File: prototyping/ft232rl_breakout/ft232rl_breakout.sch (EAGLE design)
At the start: 17 parts, among them J1 USB, U1 FT232RL

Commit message: Performed final auto routing.
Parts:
- removed L1, L2: LED, ft232rl_breakout:LED
- added D1: RED, ft232rl_breakout:LED
- added D2: GREEN, ft232rl_breakout:LED
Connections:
- net N$1 renamed VCC
- net N$16 renamed 3V3
- net VUSB renamed 5V
- net N$2: now also D1.C; no longer L1.C
- net N$3: now also D2.C; no longer L2.C
- net N$4: now also D1.A; no longer L1.A
- net N$5: now also D2.A; no longer L2.A
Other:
- note added: "1"
- note removed: "A"
- moved on the sheet: C1, C2, C3, C4, J1, JP1, JP2, JP3, JP4, JP5, JP6, JP7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

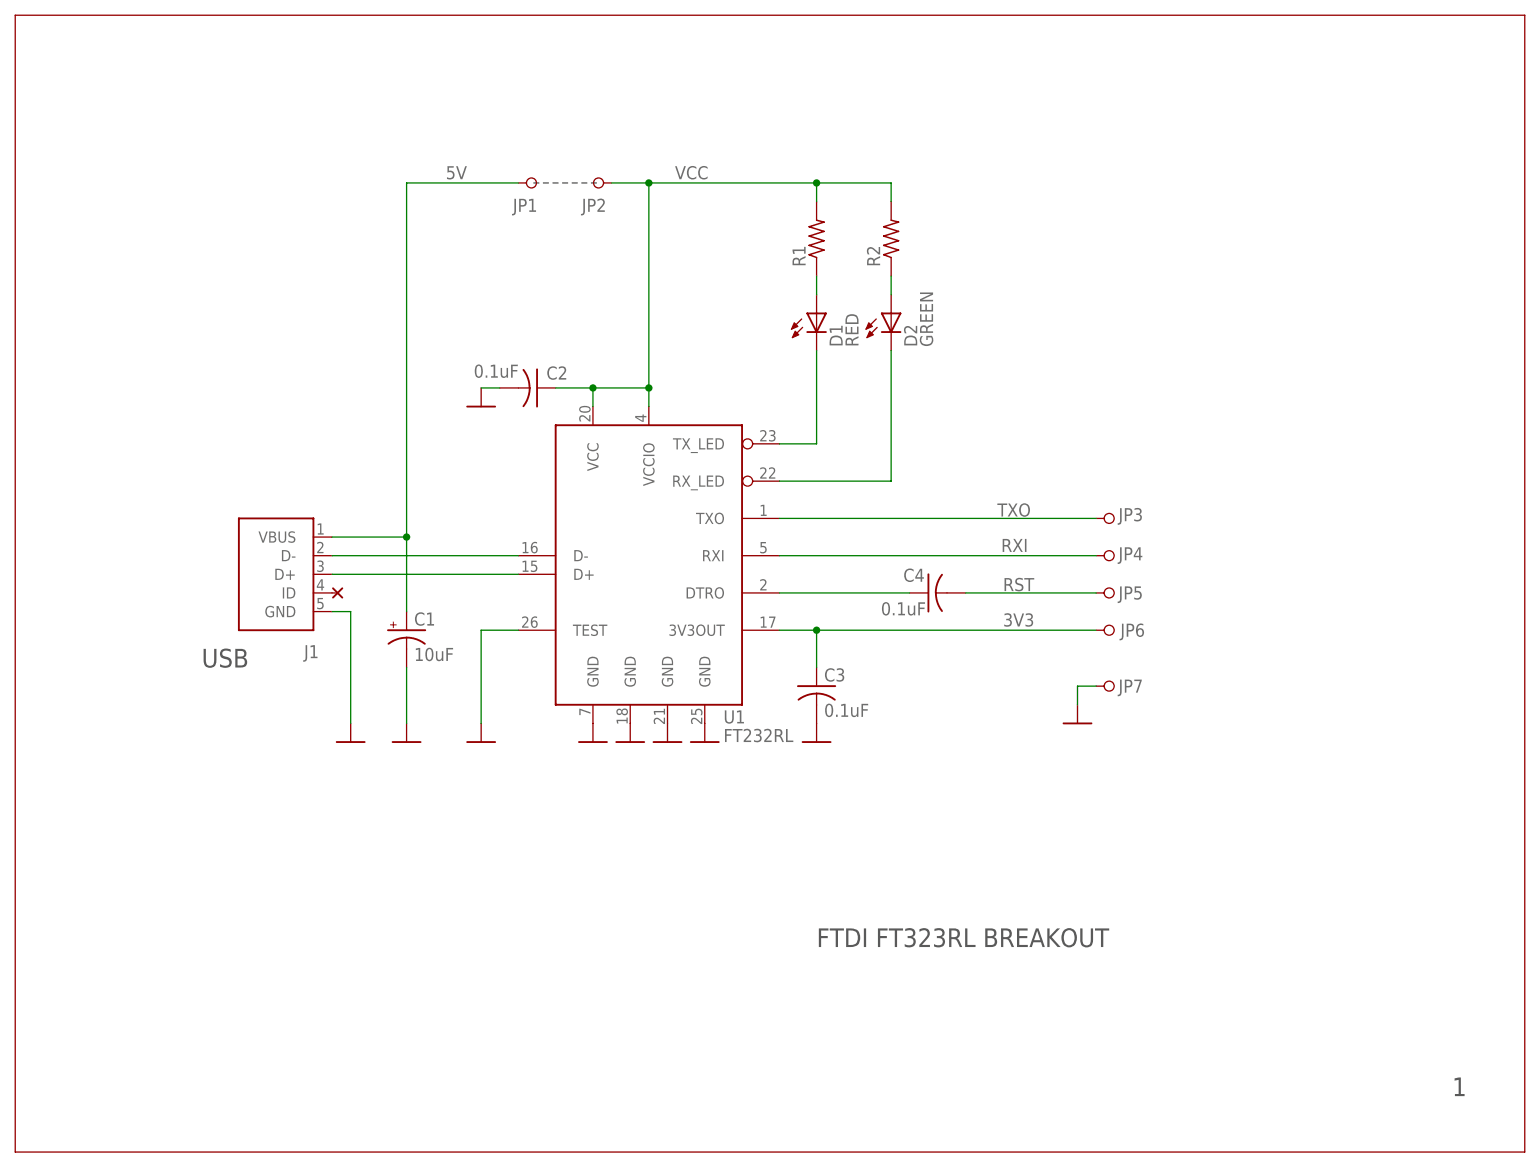
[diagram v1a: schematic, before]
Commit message: Added tcream holes for usb connector tabs. Added bom.
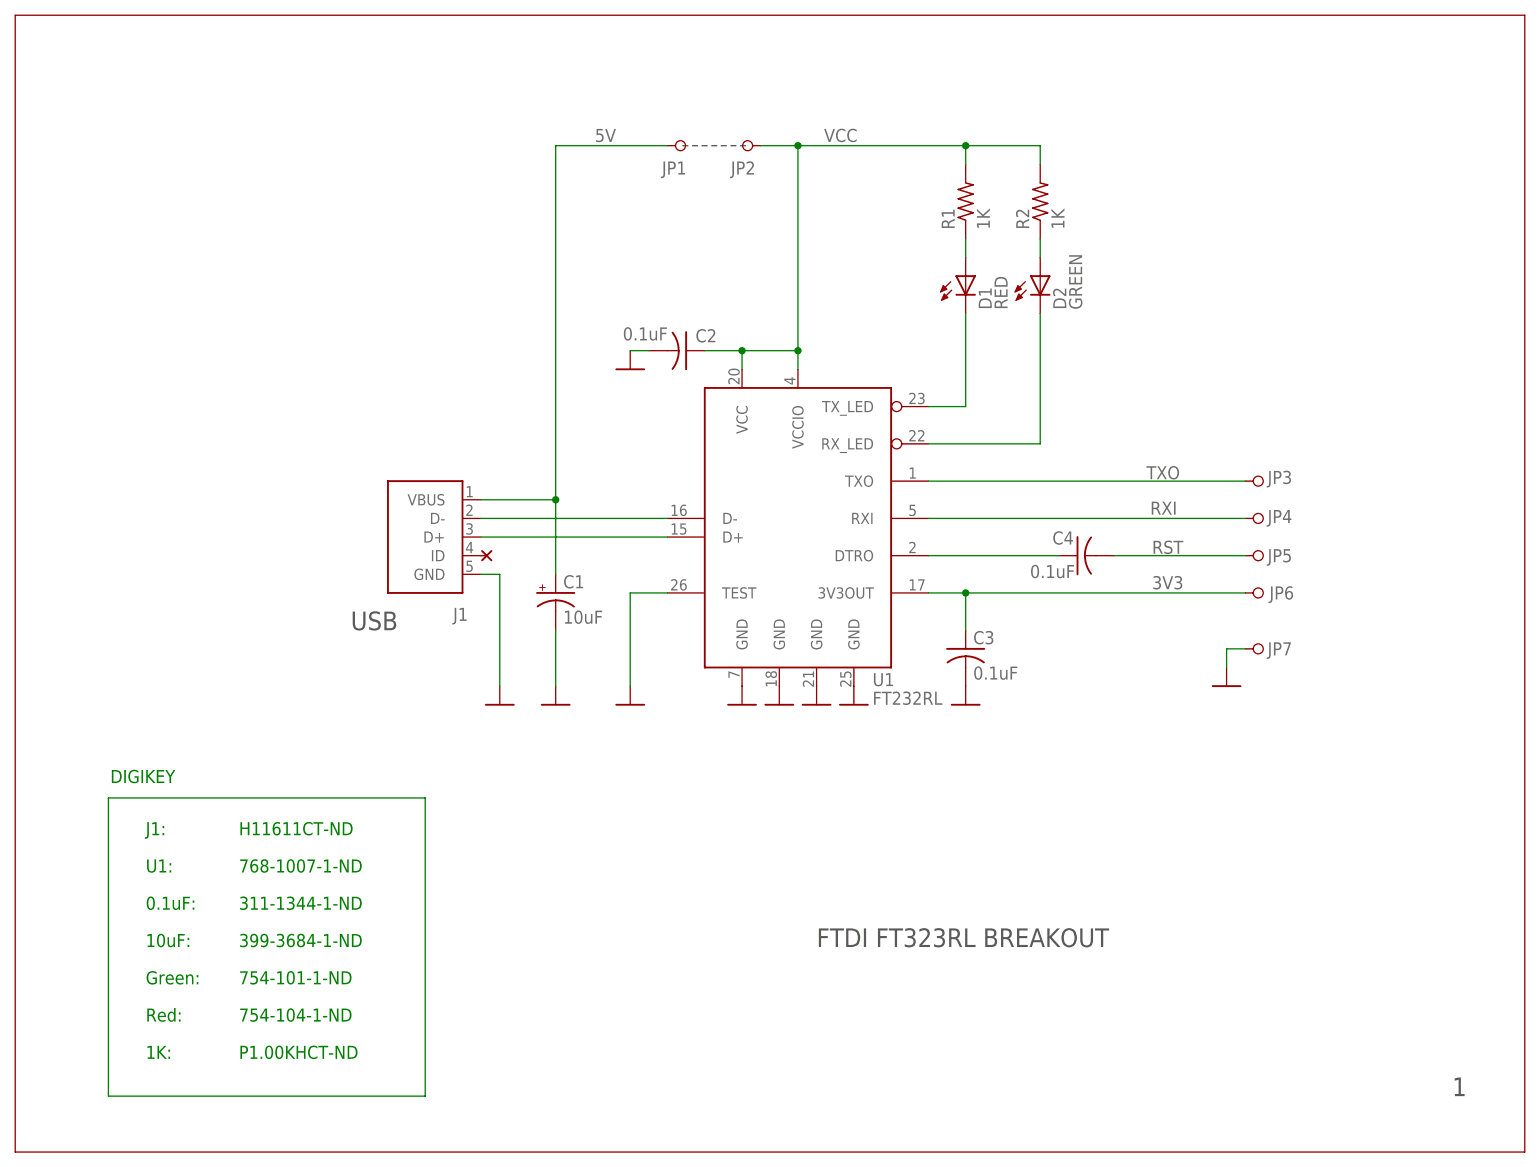
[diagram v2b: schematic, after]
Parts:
- R1, R2: value (none) -> 1K
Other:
- note added: "0.1uF:"
- note added: "10uF:"
- note added: "1K:"
- note added: "311-1344-1-ND"
- note added: "399-3684-1-ND"
- note added: "754-101-1-ND"
- note added: "754-104-1-ND"
- note added: "768-1007-1-ND"
- note added: "DIGIKEY"
- note added: "Green:"
- note added: "H11611CT-ND"
- note added: "J1:"
- note added: "P1.00KHCT-ND"
- note added: "Red:"
- note added: "U1:"
- moved on the sheet: C1, C2, C3, C4, D1, D2, J1, JP1, JP2, JP3, JP4, JP5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
